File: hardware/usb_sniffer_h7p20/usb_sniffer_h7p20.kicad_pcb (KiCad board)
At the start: 4 copper layers, 45 x 45 mm, 142 parts, among them J1 FPGA_JTAG, J2 USB_C_Receptacle_USB2.0_16P, J3 USB_A, J4 USB_C_Receptacle_USB2.0_16P, J5 FFC-40P-0.5mm,NC, J6 Trigger, U1 H7P20N0L128-M3H1, U11 EA3036C, U2 LM2903A-VR, U3 LM2903A-VR, U4 LM2903A-VR, U5 USB3343, U6 ZB25VQ16CTJG, U7 CY7C68013A-56LTX, U8 24C32, U9 CJ3439KDW, Y2 24M

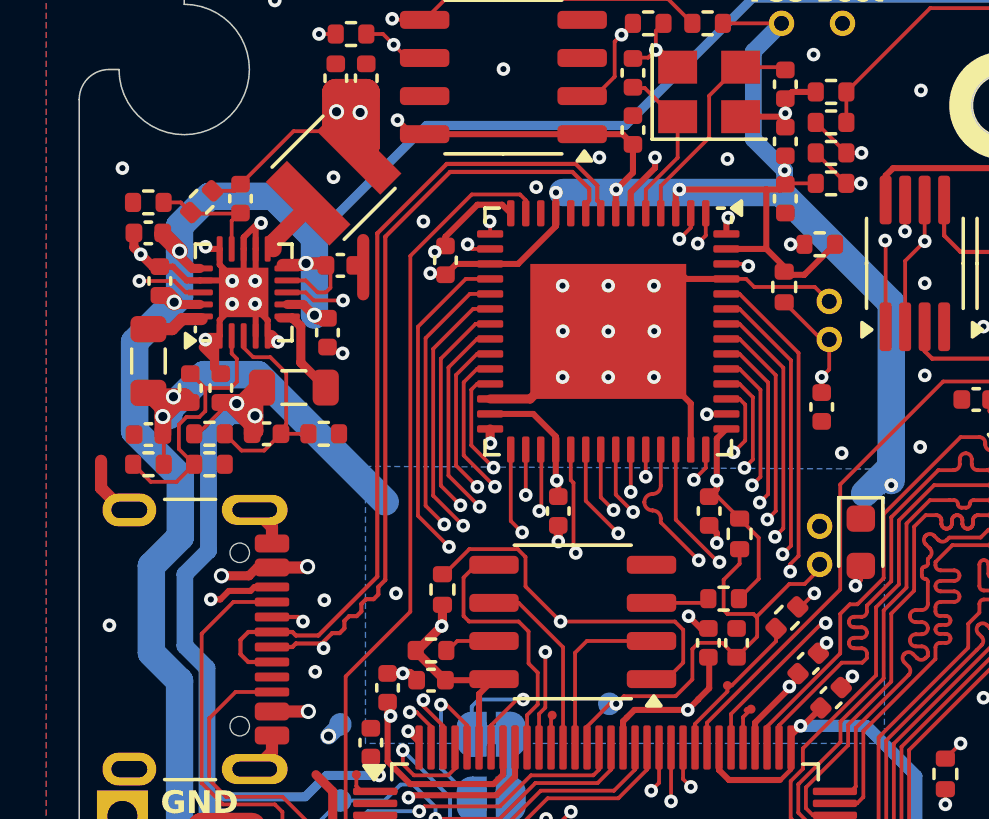
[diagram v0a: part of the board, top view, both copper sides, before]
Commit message: 将USB3343替换为CH132C，ULPI时钟由FPGA产生
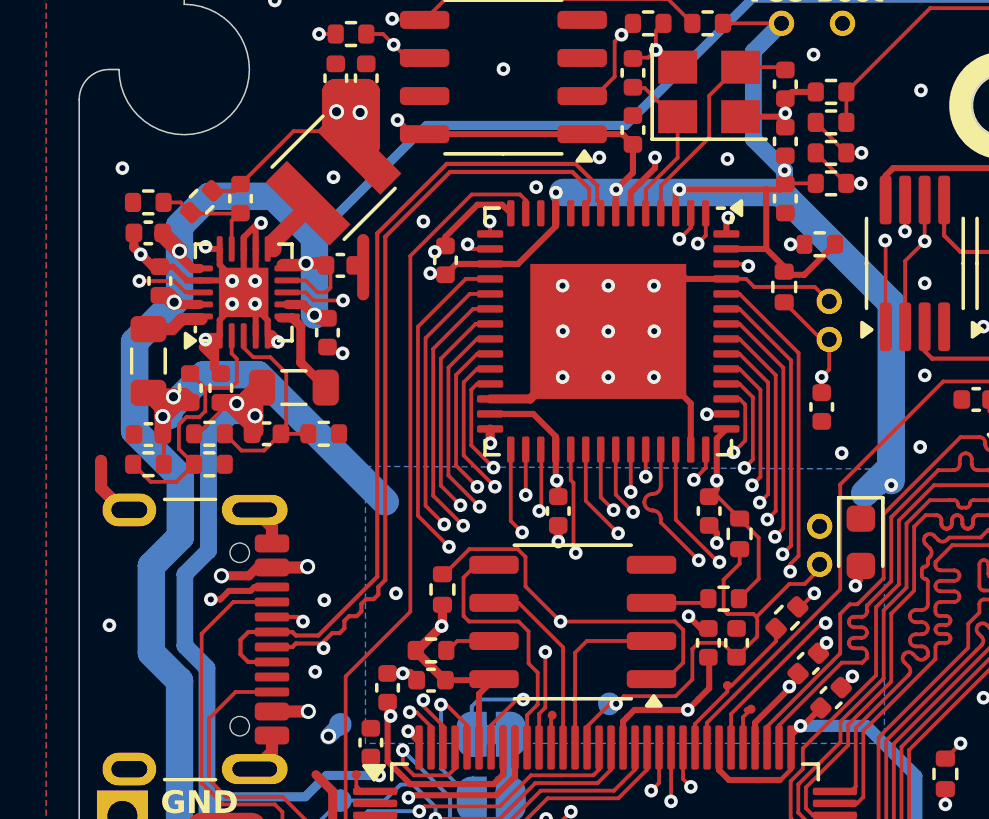
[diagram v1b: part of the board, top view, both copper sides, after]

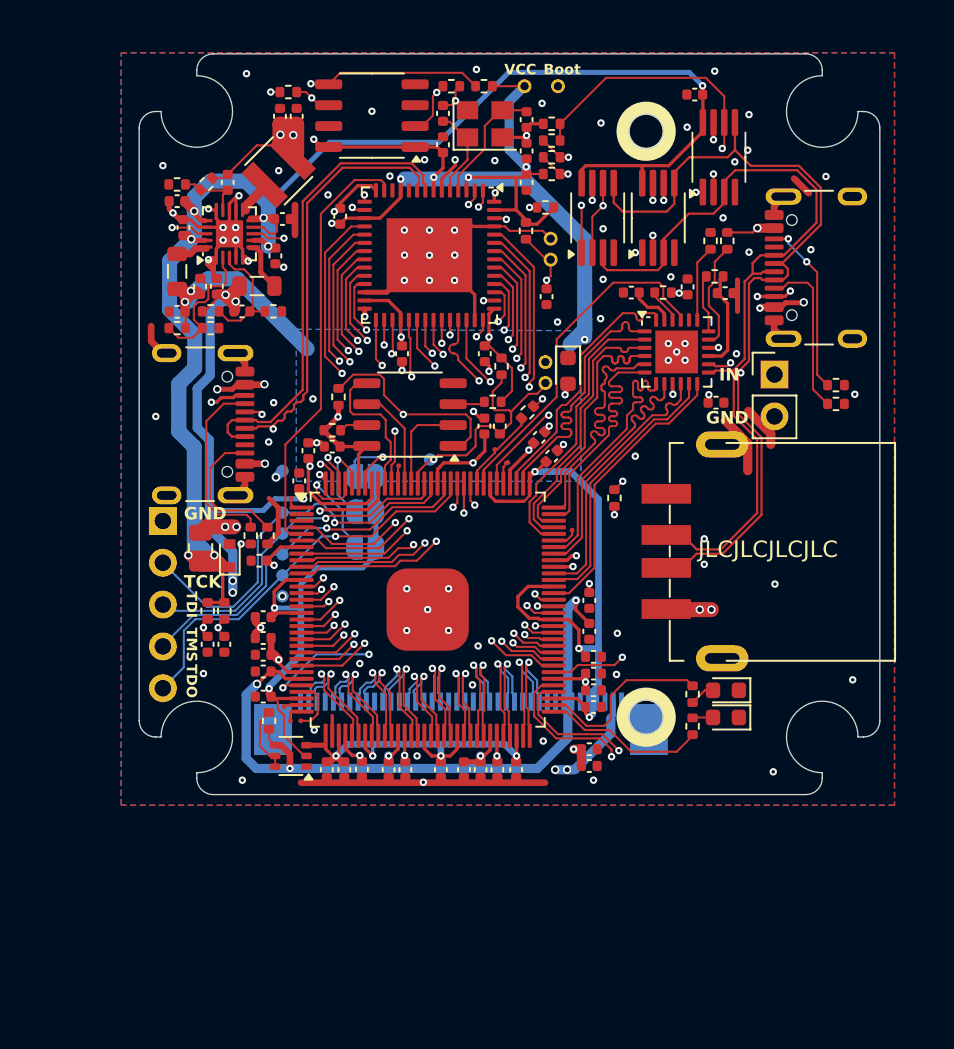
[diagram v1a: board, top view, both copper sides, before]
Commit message: [usb_sniffer_h7p20] 适配铝合金外壳、更换CH132C
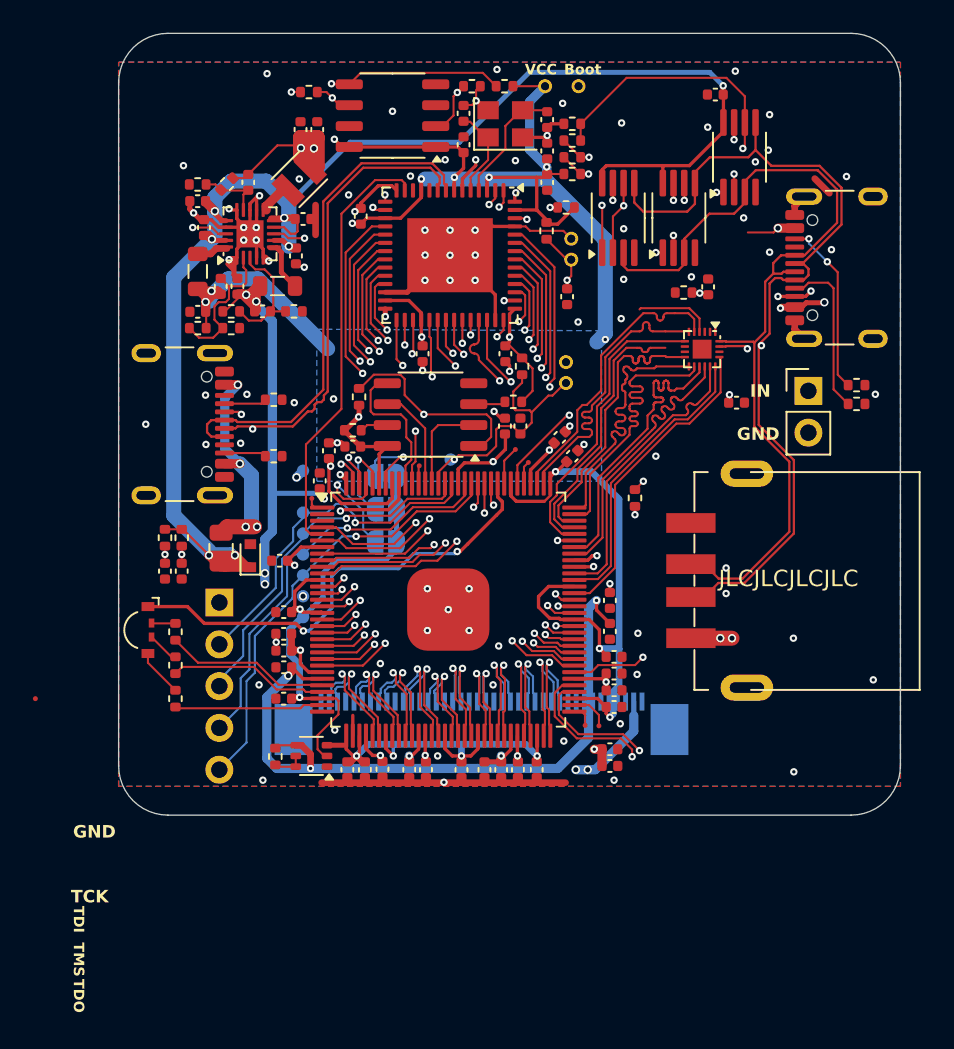
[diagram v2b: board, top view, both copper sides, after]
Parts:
- removed C10, C9: 1uF, Capacitor_SMD:C_0402_1005Metric
- removed D2: LED_RED, LED_SMD:LED_0603_1608Metric
- removed D6: LED_GREEN, LED_SMD:LED_0603_1608Metric
- removed R1: 0, Resistor_SMD:R_0402_1005Metric
- removed R28: 10k,1%, Resistor_SMD:R_0402_1005Metric
- removed R30: 8.06k,1%, Resistor_SMD:R_0402_1005Metric
- removed TP22: TestPoint, vllogic:TestPoint_Pad_D0.3mm
- removed U5: USB3343, Package_DFN_QFN:QFN-24-1EP_4x4mm_P0.5mm_EP2.6x2.6mm
- added TP19: TestPoint, vllogic:TestPoint_Pad_D0.75mm, B.Cu at (100.0, 109.2)
- added U10: CH132C, vllogic:QFN20C_2x2, F.Cu at (124.2, 92.9)
- D3: value LED_BLUE -> LED_ABGR; footprint LED_SMD:LED_0603_1608Metric -> LED_SMD:LED_RGB_Everlight_EASV3015RGBA0_Horizontal
- L5: footprint vllogic:L_NR3015 -> vllogic:L_NR2520xx
- R31: value 10k,1% -> NC
- R8: value 10k,1% -> 5.1k,1%
- moved D3 36.0 mm to (90.0, 110.0), turned to -90 degrees
- moved TP5 34.2 mm to (83.7, 114.2)
- moved R9 31.9 mm to (92.2, 110.1)
- moved R8 31.4 mm to (92.2, 114.2), turned to -90 degrees
- moved R12 26.3 mm to (92.2, 112.1), turned to -90 degrees
- moved TP21 18.3 mm to (117.1, 115.8)
- moved TP20 18.1 mm to (117.9, 115.8)
- moved R2 8.37 mm to (98.2, 96.0), turned to 180 degrees
- moved J1 6.02 mm to (94.9, 108.3)
- moved C36 5.14 mm to (91.6, 106.4)
- moved C38 5.14 mm to (92.6, 106.4)
- moved R37 5.14 mm to (92.6, 104.4)
- moved R38 5.14 mm to (91.6, 104.4)
- moved R3 4.84 mm to (98.2, 99.4), turned to 180 degrees
- moved J3 2.32 mm to (123.7, 107.0)
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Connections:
- D3 pad 1: GND -> /FPGA_CDONE
- R12 pad 1: Net-(D6-A) -> Net-(D3-GK)
- R12 pad 2: /FPGA_CDONE -> /LED_GREEN
- R31 pad 1: /VCC_3V3 -> Net-(U10-~{RESET})
- R31 pad 2: Net-(U5-~{RESETB}) -> /VCC_3V3
- R8 pad 1: Net-(D2-A) -> Net-(D3-RK)
- TP18 pad 1: /FPGA_CDONE -> Net-(U1-IO27_GCLK_2)
- TP20 pad 1: Net-(U1-IO18_7) -> Net-(U1-IO2_4)
- TP21 pad 1: Net-(U1-IO21_7) -> Net-(U1-IO1_4)
- TP5 pad 1: Net-(U1-IO12_PCLK_3) -> Net-(U1-IO22_7)
- U1 pad 104: /FPGA_OUT_26M -> Net-(U1-IO27_GCLK_2)
- U1 pad 28: /IN -> /LED_BLUE
- U1 pad 29: Net-(U1-IO18_7) -> /LED_GREEN
- U1 pad 31: Net-(U1-IO21_7) -> /LED_RED
- U1 pad 65: /LED_BLUE -> Net-(U1-IO1_4)
- U1 pad 66: /LED_RED -> Net-(U1-IO2_4)
- U1 pad 91: Net-(U1-IO12_PCLK_3) -> /IN
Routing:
- net /FPGA_CDONE: track 5.17 -> 28.1 mm, vias 0 -> 2
- net /IN: track 28.5 -> 6.88 mm, vias 3 -> 2
- net /FPGA_OUT_26M: track 21.1 -> 0.00 mm
- net GND: track 91.6 -> 71.4 mm, vias 97 -> 93
- net /LED_GREEN: track 0.00 -> 9.71 mm
- net Net-(J4-CC1): track 11.4 -> 2.58 mm
- net Net-(F1-Pad2): track 22.7 -> 14.2 mm, vias 5 -> 4
- net Net-(U5-VBUS): track 6.68 -> 0.00 mm
- net /VCC_3V3: track 191.8 -> 185.4 mm, vias 24 -> 22
- net Net-(U5-VDD33): track 6.19 -> 0.00 mm
- net Net-(J4-CC2): track 8.61 -> 2.56 mm
- net /ET3036C/EA3036_EN2: track 33.5 -> 28.4 mm
- net /VCCAUX: track 100.1 -> 95.0 mm
- net /ET3036C/EA3036_EN3: track 28.9 -> 23.8 mm
- net /USB334x_NXT: track 16.3 -> 21.0 mm
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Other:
- board size 45 x 45 mm -> 47.5 x 47.5 mm

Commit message: [usb_sniffer_h7p20] 待审查
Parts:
- moved TP5 15.9 mm to (99.6, 115.3)
- moved R7 8.13 mm to (126.3, 96.7)
- moved C8 6.74 mm to (125.2, 89.5), turned to -90 degrees
- moved R31 3.16 mm to (126.2, 89.5), turned to 90 degrees
- moved C6 0.58 mm to (124.1, 89.5)
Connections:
- U1 pad 89: /USB334x_D4 -> /IN
- U1 pad 90: /USB334x_D3 -> /USB334x_D4
- U1 pad 91: /IN -> /USB334x_DIR
- U1 pad 93: /USB334x_NXT -> /USB334x_D0
- U1 pad 94: /USB334x_D0 -> /USB334x_D3
- U1 pad 98: /USB334x_DIR -> /USB334x_STP
- U1 pad 99: /USB334x_STP -> /USB334x_NXT
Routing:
- net /IN: track 6.88 -> 15.6 mm
- net Net-(J6-Pin_1): track 12.6 -> 4.96 mm
- net Net-(U10-~{RESET}): track 0.00 -> 4.25 mm, vias 0 -> 2
- net /VCC_3V3: track 185.4 -> 181.2 mm, vias 22 -> 20
- net /VCC_5V: track 139.6 -> 143.7 mm
- net GND: track 71.4 -> 74.5 mm, vias 93 -> 101
- net /USB334x_NXT: track 21.0 -> 18.6 mm
- net Net-(U1-IO22_7): track 0.00 -> 1.69 mm
- net /USB334x_D1: track 17.1 -> 18.5 mm
- net /USB334x/T_VBUS: track 41.9 -> 40.6 mm
- net /USB334x_D4: track 17.3 -> 18.5 mm
- net /VDD_CORE: track 124.5 -> 125.7 mm
- net /USB334x_D0: track 17.4 -> 18.5 mm
- net /USB334x_D5: track 17.7 -> 18.5 mm
- net /USB334x_STP: track 17.7 -> 18.5 mm
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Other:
- board text added: "TDO TMS TDI TCK GND"
- board text added: "USB Sniffer H7P20 20250813"
- board text removed: "TCK"
- board text removed: "TDI"
- board text removed: "TDO"
- board text removed: "TMS"
- board text removed: "USB Sniffer H7P20 20250620"

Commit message: [usb_sniffer_h7p20] 20250813 打样
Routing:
- net GND: vias 101 -> 105
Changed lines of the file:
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@@
+	)
+	(via
+		(at 99.4918 98.4504)
+		(size 0.45212)
+		(drill 0.2032)
+		(layers "F.Cu" "B.Cu")
+		(free yes)
+		(net 1)
 	)
 	(via
@@
 	)
 	(via
+		(at 92.075 107.823)
+		(size 0.45212)
+		(drill 0.2032)
+		(layers "F.Cu" "B.Cu")
+		(free yes)
+		(net 1)
+	)
+	(via
 		(at 128.3008 78.6892)
 		(size 0.45212)
@@
 	)
 	(via
+		(at 124.202 92.9386)
+		(size 0.45212)
+		(drill 0.2032)
+		(layers "F.Cu" "B.Cu")
+		(net 1)
+	)
+	(via
 		(at 101.8086 95.9612)
 		(size 0.45212)
 		(drill 0.2032)
+		(layers "F.Cu" "B.Cu")
+		(free yes)
+		(net 1)
+	)
+	(via
+		(at 91.8972 116.586)
+		(size 0.45212)
+		(drill 0.2032)

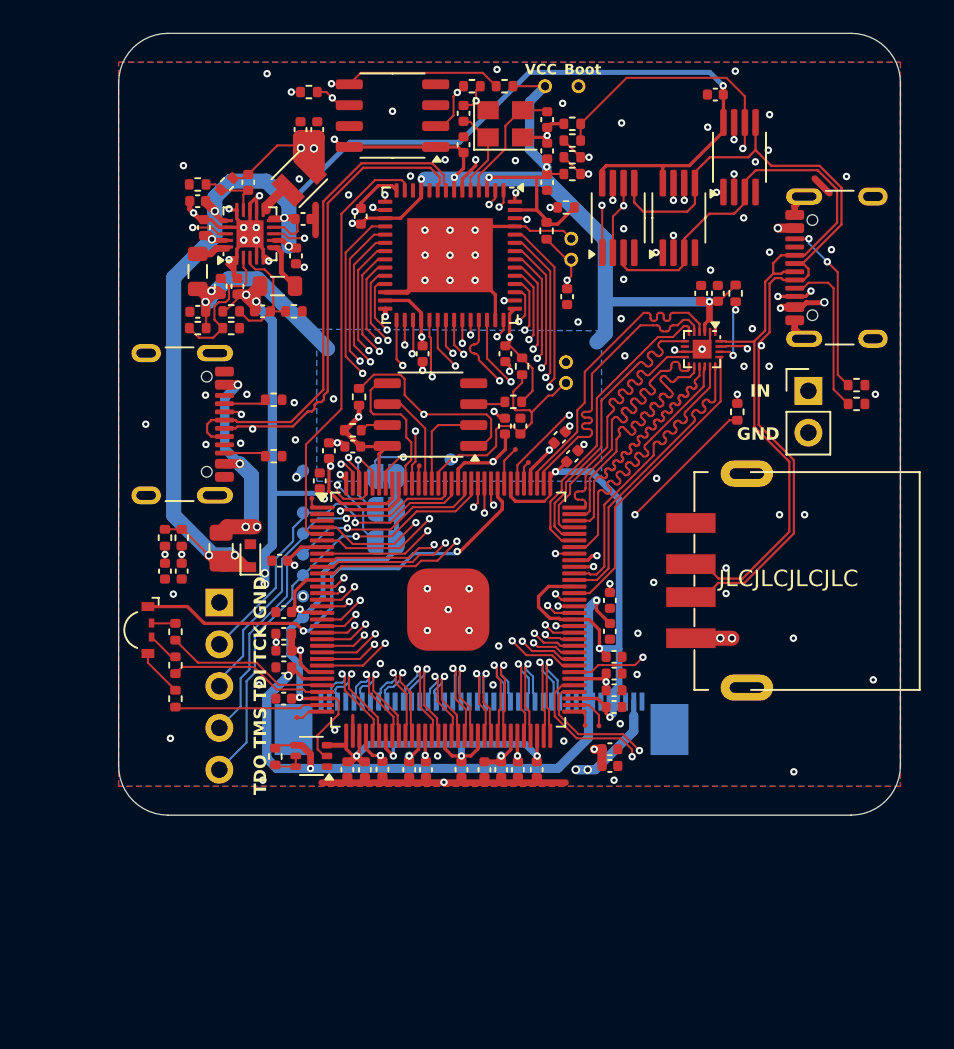
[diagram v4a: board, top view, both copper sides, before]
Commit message: [usb_sniffer_h7p20] CH132C测试无数据，回退USB3343
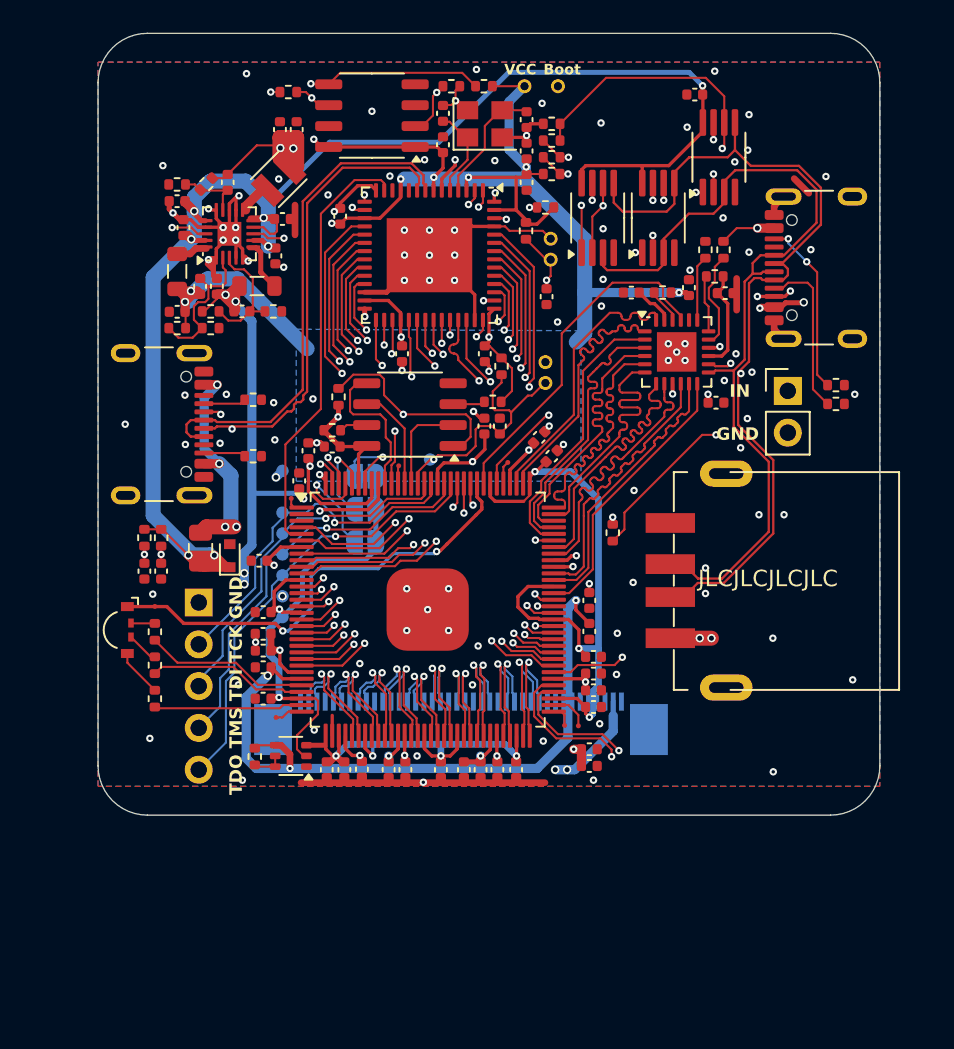
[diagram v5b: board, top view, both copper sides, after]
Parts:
- removed U10: CH132C, vllogic:QFN20C_2x2
- added C10: 1uF, Capacitor_SMD:C_0402_1005Metric, F.Cu at (125.6, 89.5)
- added C9: 1uF, Capacitor_SMD:C_0402_1005Metric, F.Cu at (119.9, 89.5)
- added R1: 0, Resistor_SMD:R_0402_1005Metric, F.Cu at (125.0, 88.5)
- added R28: 10k,1%, Resistor_SMD:R_0402_1005Metric, F.Cu at (125.5, 86.9)
- added R30: 8.06k,1%, Resistor_SMD:R_0402_1005Metric, F.Cu at (124.4, 86.9)
- added U5: USB3343, vllogic:QFN-24-1EP_4x4mm_P0.5mm_EP2.6x2.6mm, F.Cu at (122.7, 93.1)
- R31: value NC -> 10k,1%
- R8: value 5.1k,1% -> 10k,1%
- U11: footprint Package_DFN_QFN:QFN-20-1EP_3x3mm_P0.4mm_EP1.65x1.65mm -> vllogic:QFN-20-1EP_3x3mm_P0.4mm_EP1.65x1.65mm
- moved TP18 23.9 mm to (91.0, 108.6)
- moved R7 10.5 mm to (118.8, 104.1), turned to -90 degrees
- moved C8 6.64 mm to (125.0, 96.2), turned to 180 degrees
- moved R31 4.44 mm to (121.8, 89.5), turned to 180 degrees
- moved C11 1.25 mm to (101.7, 98.9)
- moved C12 1.25 mm to (117.6, 113.7)
- moved C13 1.25 mm to (109.7, 118.5)
- moved C14 1.25 mm to (97.5, 108.9)
- moved C15 1.25 mm to (117.6, 112.6)
- moved C16 1.25 mm to (99.7, 100.9)
- moved C17 1.25 mm to (94.7, 89.1)
- moved C18 1.25 mm to (111.0, 97.6)
- moved C19 1.25 mm to (117.3, 117.2)
- moved C2 1.25 mm to (111.9, 97.6)
- moved C20 1.25 mm to (92.3, 90.7)
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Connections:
- R31 pad 1: Net-(U10-~{RESET}) -> /VCC_3V3
- R31 pad 2: /VCC_3V3 -> Net-(U5-~{RESETB})
- TP18 pad 1: Net-(U1-IO27_GCLK_2) -> /FPGA_CDONE
- U1 pad 104: Net-(U1-IO27_GCLK_2) -> /FPGA_OUT_26M
- U1 pad 89: /IN -> /USB334x_D4
- U1 pad 90: /USB334x_D4 -> /USB334x_D3
- U1 pad 91: /USB334x_DIR -> /IN
- U1 pad 93: /USB334x_D0 -> /USB334x_NXT
- U1 pad 94: /USB334x_D3 -> /USB334x_D0
- U1 pad 98: /USB334x_STP -> /USB334x_DIR
- U1 pad 99: /USB334x_NXT -> /USB334x_STP
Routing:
- net /FPGA_OUT_26M: track 0.00 -> 21.1 mm
- net Net-(J6-Pin_1): track 4.96 -> 15.0 mm
- net /IN: track 15.6 -> 6.84 mm
- net /VCC_3V3: track 181.2 -> 187.9 mm, vias 20 -> 23
- net Net-(U5-VDD33): track 0.00 -> 6.20 mm
- net Net-(U5-VBUS): track 0.00 -> 6.00 mm
- net Net-(U10-~{RESET}): track 4.25 -> 0.00 mm, vias 2 -> 0
- net Net-(U5-RBIAS): track 0.00 -> 3.96 mm
- net Net-(U5-ID): track 0.00 -> 3.48 mm
- net Net-(U5-VDD18): track 0.00 -> 2.45 mm
- net /USB334x/T_VBUS: track 40.6 -> 42.9 mm
- net Net-(U1-IO27_GCLK_2): track 2.35 -> 0.00 mm
- net Net-(U5-~{RESETB}): track 0.00 -> 2.13 mm
- net /USB334x_DIR: track 18.6 -> 16.7 mm
- net /USB334x_D1: track 18.5 -> 16.7 mm
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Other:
- board text added: "USB Sniffer H7P20 20250818"
- board text removed: "USB Sniffer H7P20 20250813"

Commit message: [usb_sniffer_h7p20] 统一使用P25Q64SH-SSH-IR
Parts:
- U6: value ZB25VQ16CTJG -> P25Q64SH-SSH-IR
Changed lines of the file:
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@@
 			)
 		)
-		(property "Value" "ZB25VQ16CTJG"
+		(property "Value" "P25Q64SH-SSH-IR"
 			(at 0 3.4 0)
 			(layer "F.Fab")
